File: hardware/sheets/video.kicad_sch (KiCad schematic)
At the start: 28 parts, among them J1 HDMI_A, J2 VGA HD15, M1 Core2350B (8MB PSRAM), U2 74LVC245A, U3 74LVC245A, U4 74LVC245A, U5 74LVC245A, U6 74LVC245A, U7 74LVC245A

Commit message: JLCPCB sourcing pass: verify pinouts, LCSC part numbers, SMD build
Custom-symbol verification (open-questions Q5 resolved):
- MAX3241 symbol was wrong on nearly every pin and used MAX3243-style
  control names; regenerated to the real SSOP-28 pinout (SHDN#/EN#/
  R1OUTB/R2OUTB) and com_port rewired -- EN# must be GROUNDED (the old
  ~FORCEON-high would have disabled the receivers on real silicon)
- DS12C887 symbol wrong on 4 pins (DS=17, RESET#=18, IRQ#=19, SQW=23)

Sourcing (every part checked against the JLC DB; ~45 line items):
- New tools/parts.py maps (lib_id, value) -> LCSC; build.py applies it as
  an 'LCSC Part Num' property on every component (384 across the project)
- Sheets stay generic; stock-forced substitutions bound in the map:
  '374->'574 (parallel rewired), '163->'161, '157->HC157 (+HCT-buffered
  3.3V selects, I0/I1 swapped), '02->HC02, TCM809->MCP809, 2N3904->MMBT3904
- bus_mcu address counters moved to the 3.3V domain (HC161 on 3V3_BUS,
  loaded from MCU-side MD0-7; HCT244s read the 3.3V outputs at TTL Vih)
- 14.318 XOs are 3.3V-only parts: powered from 3V3, squared up via spare
  HCT gates (cpu_core U13, card_isatest U19)
- COM baud reference is now a 1.8432MHz crystal on the 16C550's XIN/XOUT
  (3.3V-only oscillators vs a 5V-only soft card)
- Supervisor QSPI header replaced with a real W25Q128JVSIQ
- Socket policy (fab installs sockets): V20 DIP-40, SRAM DIP-32 (no 5V
  512Kx8 SRAM at JLC at all), DS12C887 DIP-24, female headers for modules

Docs: CLAUDE.md fabrication-constraints section (SMD, 100x100mm, generic-
symbols rule, voltage-domain rule); README + hardware/README fab notes;
notes/jlcpcb-sourcing.md (decisions, thin-stock flags, not-at-JLC list);
stale questions-sidecar.md collapsed to its supersession record.

Rebuilt motherboard + cards: structural ERC 0, byte-identical rebuilds.

Co-Authored-By: Claude Fable 5 <noreply@anthropic.com>
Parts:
- C1, C2: LCSC Part Num (none) -> C14663
- C3: LCSC Part Num (none) -> C15850
- J1: LCSC Part Num (none) -> C2858275
- M1: LCSC Part Num (none) -> C2897411
- R10, R11, R12, R13, R14, R15, R16, R17: LCSC Part Num (none) -> C22966
- R20, R23: LCSC Part Num (none) -> C22975
- R21, R24, R26: LCSC Part Num (none) -> C21190
- R22, R25, R27: LCSC Part Num (none) -> C23193
- U2, U3, U4, U5, U6, U7: LCSC Part Num (none) -> C6082

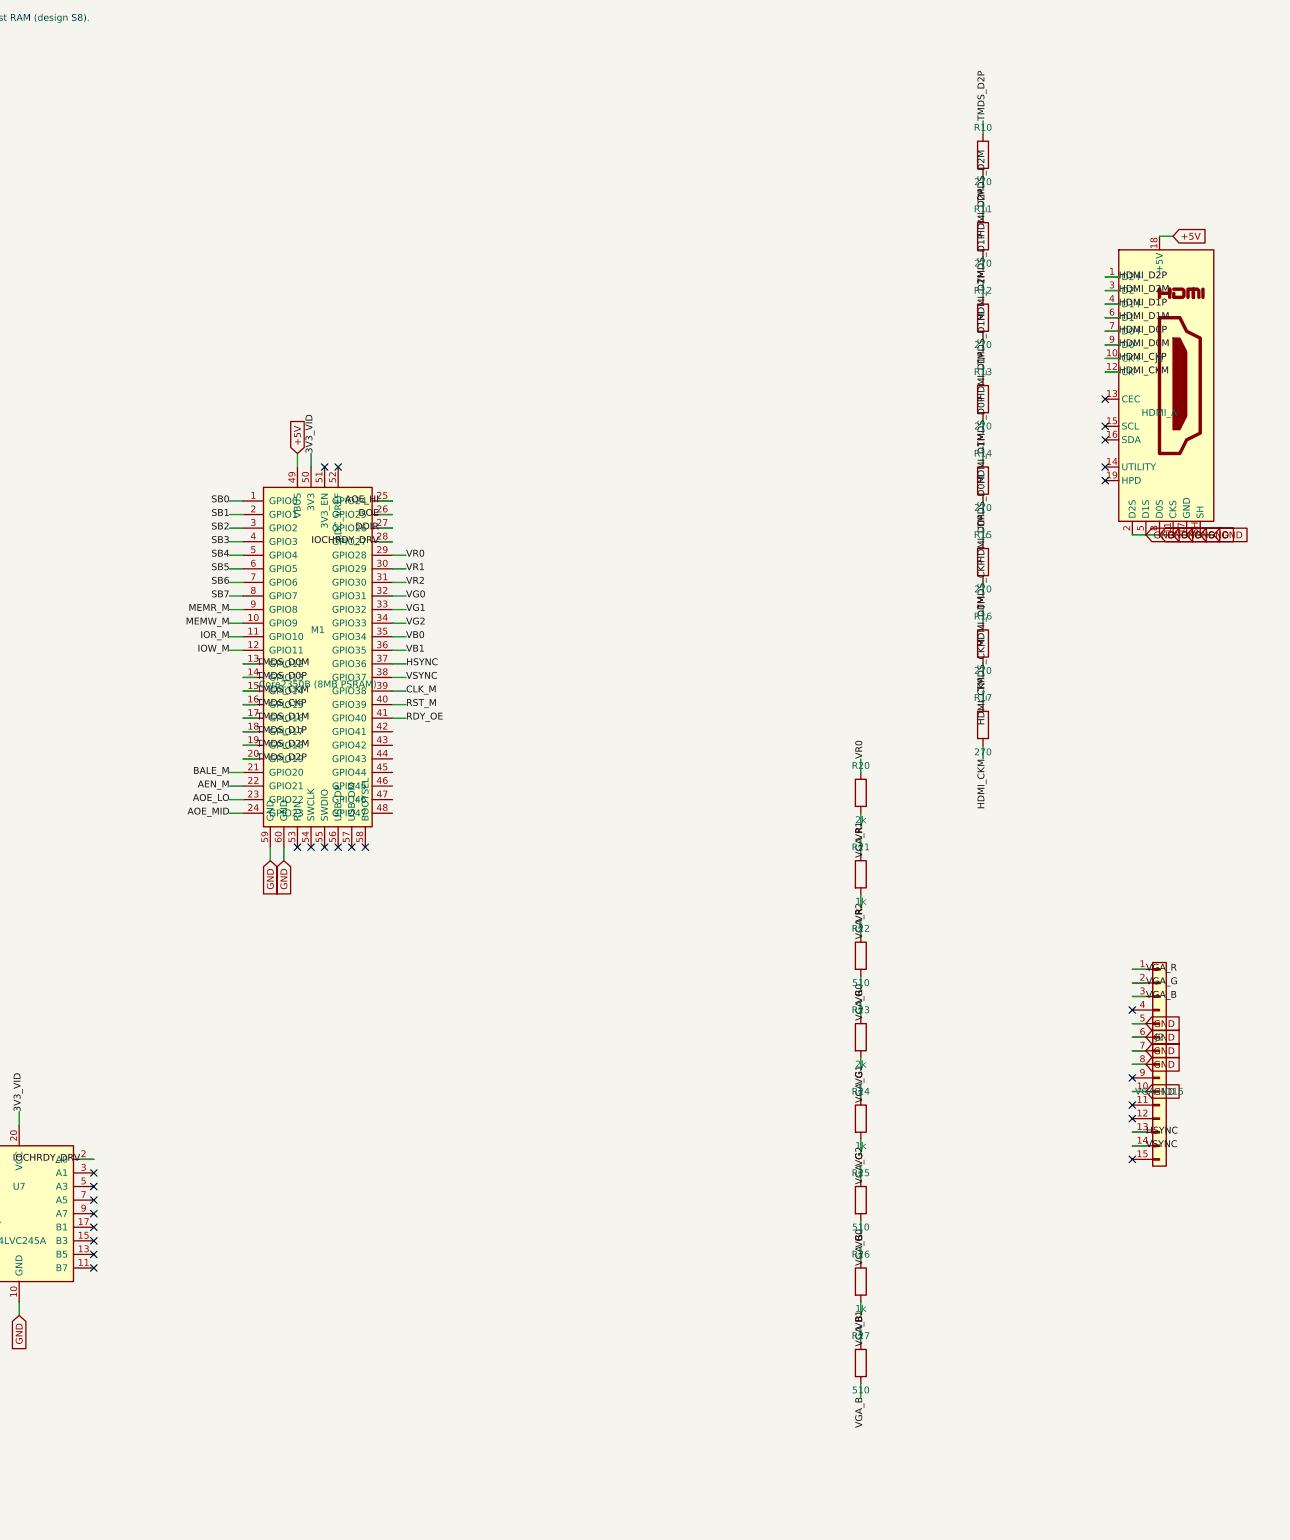
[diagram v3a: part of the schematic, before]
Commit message: Design review 2026-07-11: rail protection, decoupling, wiring fixes
Protection:
- Sidecar +5V now feeds through a 2A polyfuse into +5V_ISA with an
  SMBJ5.0A clamp + 22uF bulk (a faulted ISA card trips its own fuse
  instead of dropping the board; back-fed voltage is clamped).
- USB-C VBUS enters through a 3A polyfuse with an SMBJ5.0A on +5V
  (backstop for the CFG1 9-20V failure mode). CH224K gains a 1uF VDD
  cap; its PG routes to Supervisor GPIO16 as PD_PG. Buck output
  doubled to 2x22uF, 10uF at VIN, extra rail bulk.
- Supervisor USB-A host port: 27R series termination (RP2040
  requirement), USBLC6-2SC6 ESD array, 100uF VBUS bulk.
- Video: HDMI +5V fused (500mA), HPD sensed on GPIO41, 100R series on
  VGA sync. TMDS ESD array deferred to layout (no symbol).
- card_isatest: V5RAW bulk, Q1 gate soft-start cap, TVS on DUT rail.

Wiring fixes:
- SPKR had no driver anywhere (netlist: 1 node). Bus MCU GPIO22
  reassigned from the diagnostics-only bus-CLK sense to SPKR; bus_mcu
  drops CLK from its interface. Doc 5.2 updated.
- bus_mcu C8 decoupled +3V3, a rail that sheet never uses -> 3V3_BUS.
- Storage IRQ5 was push-pull (permanently driven when idle) -> 2N7002
  + gated '125 tri-state, same convention as the LPT IRQ7 stage.
- MAX3241 pump caps resized to the 5V datasheet values (47nF/330nF).
- LPT DB25 status inputs get 4.7k pull-ups (floated with no printer).
- Audio line-out gets a 100R series isolator before the jack.

Best practices:
- Decoupling to ~1x100nF per IC on every sheet + bulk per board
  (cpu_core 7->16 incl. the naked 3.3V oscillator, storage 4->11,
  parallel 6->13, rtc/com/video/bus_mcu/card_isatest similar).
- All floating spare CMOS inputs tied ('00/'74/'157/'02/'04/'125
  sections across cpu_core, bus_mcu, rtc, storage, card_isatest).

Sourcing: new parts mapped in parts.py with JLC-verified LCSC numbers;
Power_Protection lib registered in the tools; TPS563200 stock alert
(4 pcs left at JLC) flagged in parts.py + jlcpcb-sourcing.md. All
decisi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
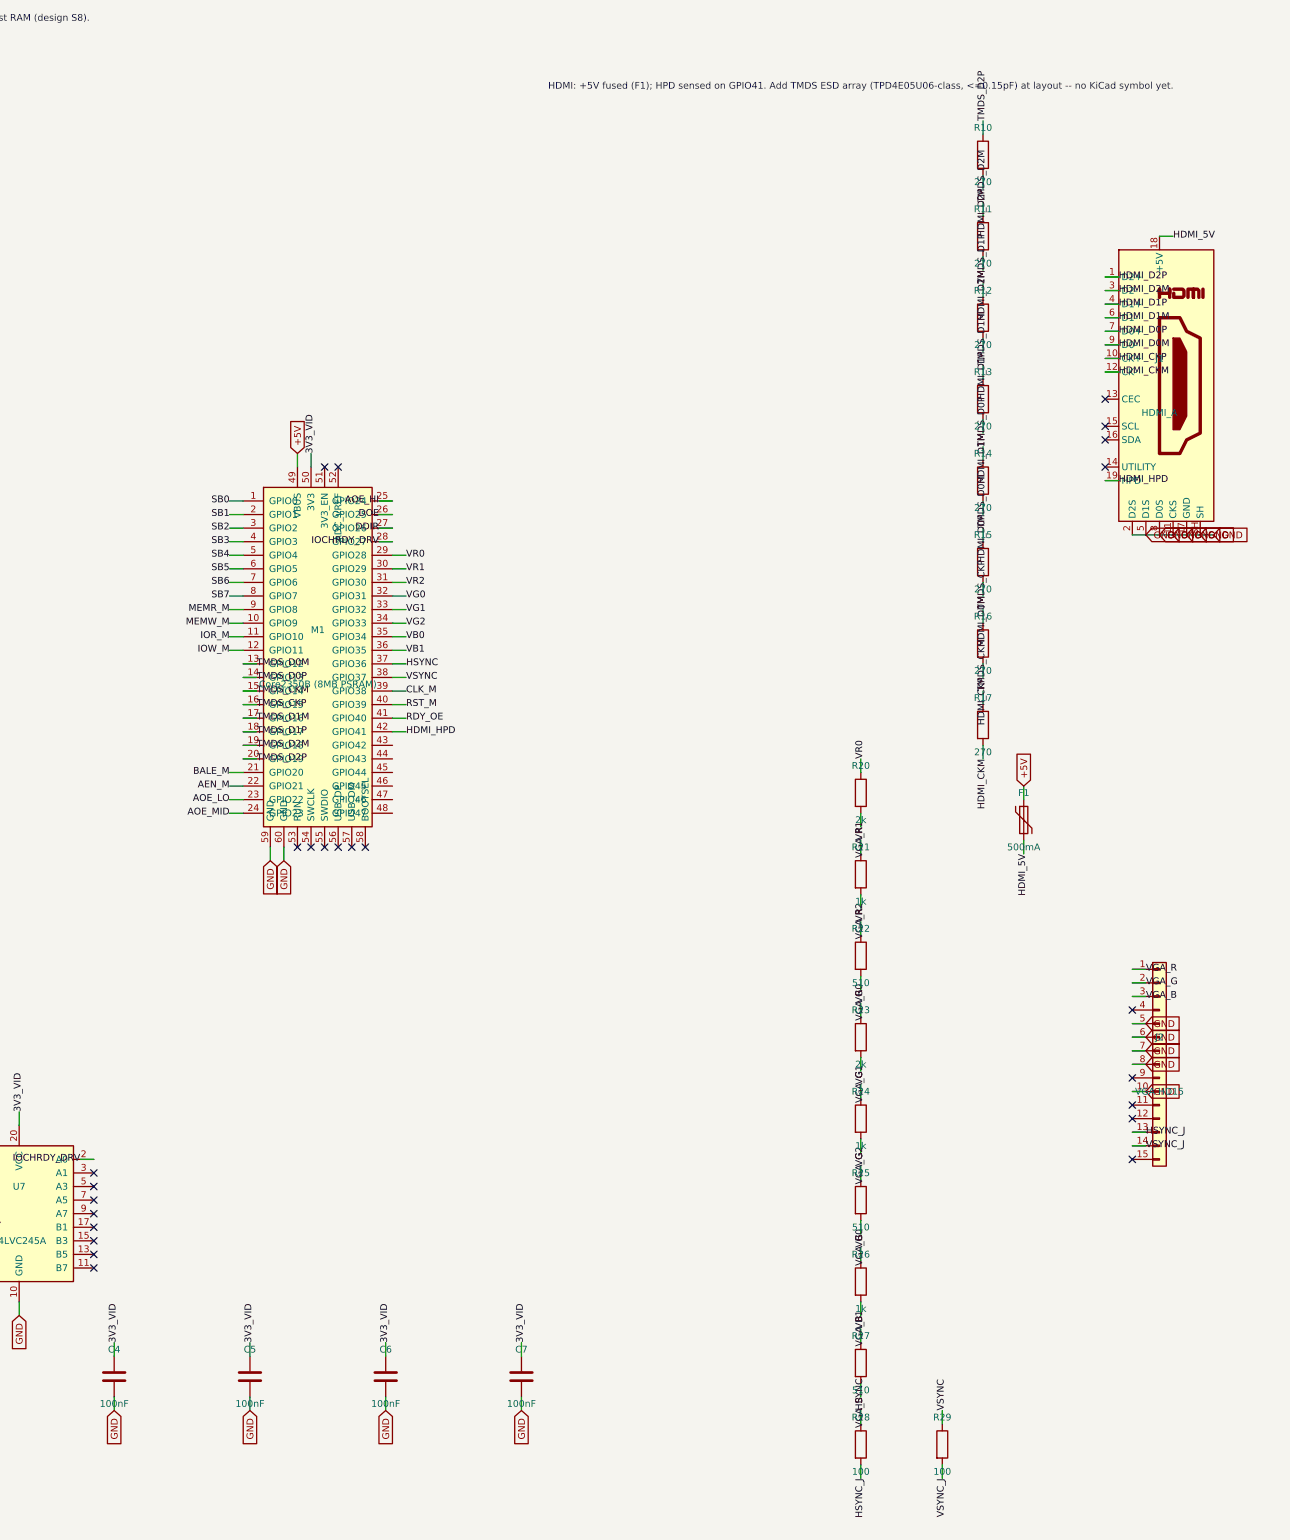
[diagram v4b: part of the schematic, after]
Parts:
- added C4, C5, C6, C7: 100nF, symbol Device:C
- added R13: 270, symbol Device:R
- added R28, R29: 100, symbol Device:R
- F1: renamed from R13; value 270 -> 500mA; symbol Device:R -> Device:Polyfuse; LCSC Part Num C22966 -> C46641014
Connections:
- net +5V: now also F1.1; no longer J1.18 (+5V)
- net 3V3_VID: now also C4.1, C5.1, C6.1, C7.1
- net GND: now also C4.2, C5.2, C6.2, C7.2
- net HDMI_D1M: now also R13.2; no longer F1.2
- net HSYNC: now also R28.1; no longer J2.13 (Pin_13)
- net TMDS_D1M: now also R13.1; no longer F1.1
- net VSYNC: now also R29.1; no longer J2.14 (Pin_14)
- net HDMI_HPD: now reaches M1.42 (GPIO41)
- net HDMI_HPD: now also J1.19 (HPD)
- new net HDMI_5V: F1.2, J1.18 (+5V)
- new net HSYNC_J: J2.13 (Pin_13), R28.2
- new net VSYNC_J: J2.14 (Pin_14), R29.2
- no-connect marks 40 -> 39
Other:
- note added: "HDMI: +5V fused (F1); HPD sensed on GPIO41. Add TMDS ESD array (TPD4E05U06-class, <=0.15pF) at layout -- no KiCad symbol yet."

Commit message: Storage/video: enable + base-address straps
Completes the jumper story started with COM/LPT: every on-board peripheral
can now be disabled or re-strapped to make room for the same card on the
sidecar chain.

- storage: JP1 base 0x300/0x320 (differ only in A5; A5_SEL replaces nA5 in
  the HI_MATCH tree, XTIDE UB supports both) and JP2 enable on DEC1's spare
  ~E1 (open kills /CS0 + /ODD_SEL, so DEC2/DEC3, both high-byte latches and
  the low-byte '245 go inert; INTRQ's pull-down keeps IRQ5 released). Same
  pattern as the LPT sheet.
- video: firmware-read boot straps -- this snoop card decodes in firmware,
  so there is no hardware chip-select to gate. JP1/VID_EN (GPIO42, 10k to
  3V3_VID) open = firmware keeps every bus-facing OE off (all drivers are
  MCU-gated tri-states, so a disabled card is electrically silent);
  JP2/VID_BASE (GPIO43) closed = CGA windows (0x3D4/0xB8000), open =
  MDA/Hercules (0x3B4/0xB0000) -- the snoop equivalent of a period card's
  MDA/CGA switch.

Design doc updated (8, 10, 14 I/O map); decisions logged in
questions-storage.md / questions-video.md.

Verified: motherboard + cards rebuild with zero structural ERC; netlist
ties each strap to its jumper, pull resistor and decode/GPIO pin
(A5_SEL/~{STOR_EN} on storage, VID_EN/VID_BASE on the video module).

Co-Authored-By: Claude Fable 5 <noreply@anthropic.com>
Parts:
- added JP1: VID_EN, symbol Connector_Generic:Conn_01x02
- added JP2: VID_BASE, symbol Connector_Generic:Conn_01x02
- added R30, R31: 10k, symbol Device:R
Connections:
- net 3V3_VID: now also R30.1, R31.1
- net GND: now also JP1.2 (Pin_2), JP2.2 (Pin_2)
- net VID_EN: now reaches M1.43 (GPIO42)
- net VID_EN: now also JP1.1 (Pin_1), R30.2
- net VID_BASE: now reaches M1.44 (GPIO43)
- net VID_BASE: now also JP2.1 (Pin_1), R31.2
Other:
- note added: "SOFT CARD: ISA bus + power ONLY. Self-decodes 0xA0000-0xBFFFF and 3B4/3B5/3B8/3BA/3BF + 3D4/3D5/3D8/3D9/3DA from snooped A17-A19/A0-A9. No Y5, no link, no host RAM (design S8). Straps: JP1 open = card disabled (firmware keeps all OEs off); JP2 = CGA (closed) / MDA (open) window set."
- note removed: "SOFT CARD: ISA bus + power ONLY. Self-decodes 0xA0000-0xBFFFF and 3B4/3B5/3B8/3BA/3BF + 3D4/3D5/3D8/3D9/3DA from snooped A17-A19/A0-A9. No Y5, no link, no host RAM (design S8)."
